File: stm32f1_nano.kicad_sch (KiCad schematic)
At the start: 48 parts, among them J1 Analog, J2 Digital, J3 TYPE-C-31-M-12, J4 Conn_ST_STDC14, Q1 AO3401A, Q3 AO3401A, U1 STM32F103C8T6, U2 W25Q32JVSS, U3 AMS1117-3.3, U5 AMS1117-5.0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

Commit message: First draft almost done
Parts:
- added J5: DEBUG, Connector_PinHeader_2.54mm:PinHeader_1x04_P2.54mm_Vertical, symbol Connector_Generic:Conn_01x04
- C15, C16, D7, J4, Q3, R11, U5: now not fitted
- J1, J2: now left out of the parts list
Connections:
- net GND: now also J5.1 (Pin_1)
- net SWCLK: now also J5.3 (Pin_3)
- net SWDIO: now also J5.4 (Pin_4)
- net SWO: now also J5.2 (Pin_2)
- net ~{RESET}: no longer J2.13 (Pin_13)
- no-connect marks 6 -> 7
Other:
- moved on the sheet: JP1

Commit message: New PS
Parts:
- removed JP1: Disc. VBUS, Jumper:SolderJumper-2_P1.3mm_Bridged_RoundedPad1.0x1.5mm, symbol Jumper:SolderJumper_2_Bridged
- added C17, C18: 1u 25V, Capacitor_SMD:C_0402_1005Metric, symbol Device:C_Small
- added D8: LED red (PWR), LED_SMD:LED_0603_1608Metric, symbol Device:LED_Small
- added D9: 1N5819WS, Diode_SMD:D_SOD-323, symbol Device:D_Schottky_Small
- added R12: 1k5, Resistor_SMD:R_0402_1005Metric, symbol Device:R_Small
- added U4: XC6206P332MR, Package_TO_SOT_SMD:SOT-23-3, symbol Regulator_Linear:XC6206PxxxMR
- C13, C14, D5, D6, Q1, R10, R9, U3: now not fitted; now left out of the parts list
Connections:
- net VBUS is gone; now on net +5V: Q1.3 (D)
- net +3.3V: now also C18.1, D8.2 (A), U4.2 (VO)
- net +5V: now also C17.1, D9.1 (K), U4.3 (VI)
- net GND: now also C17.2, C18.2, R12.2, U4.1 (GND)
- net VBUS0: now reaches J3.A4 (VBUS), J3.A9 (VBUS), J3.B4 (VBUS), J3.B9 (VBUS)
- net VBUS0: now also D9.2 (A)
- new net: D8.1 (K), R12.1
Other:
- note added: "3V3 Power Supply (Input: 15V)"
- note removed: "3V3 Power Supply"
- moved on the sheet: C15, C16, D7, JP2, Q3, R11, U5

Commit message: Reassigned Pins
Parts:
- removed C11: 20p 50V, Capacitor_SMD:C_0603_1608Metric, symbol Device:C_Small
- removed D7: 6V, Diode_SMD:D_MiniMELF, symbol Device:D_Zener_Small
- removed X1: NX3225GD-8MHZ-STD-CRA-3, Project_Library:NX3225GD8MHZSTDCRA3, symbol Project_Library:NX3225GD-8MHZ-STD-CRA-3
- added C19: 20p 50V, Capacitor_SMD:C_0402_1005Metric, symbol Device:C_Small
- added D10: SMF6.0CA, Diode_SMD:D_SOD-123F, symbol Device:D_Zener_Small
- added U6: SRV05-4, Package_TO_SOT_SMD:SOT-23-6, symbol Power_Protection:SRV05-4
- added Y1: X322516MLB4SI, Crystal:Crystal_SMD_3225-4Pin_3.2x2.5mm, symbol Device:Crystal_GND24_Small
- C10: footprint Capacitor_SMD:C_0603_1608Metric -> Capacitor_SMD:C_0402_1005Metric; JLCPCB Part # C1648 -> C1554; Manufacturer Samsung Electro-Mechanics -> FH (Guangdong Fenghua Advanced Tech); Partnumber CL10C200JB8NNNC -> 0402CG200J500NT
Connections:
- net +5V: now also D10.1 (K)
- net GND: now also C19.1, Y1.2, Y1.4
- net HSE_IN: now also C19.2, Y1.1; no longer C10.2
- net HSE_OUT: now also C10.2, Y1.3
- net LED2_ORG: now also U1.3 (PC14); no longer U1.38 (PA15)
- net LED3_RED: now also U1.29 (PA8); no longer U1.21 (PB10)
- net LED4_BLU: now also U1.20 (PB2); no longer U1.22 (PB11)
- net PB4: now also J2.10 (Pin_10); no longer J2.9 (Pin_9)
- net PB5: now also J2.9 (Pin_9); no longer J2.8 (Pin_8)
- net PB6: now also J2.8 (Pin_8); no longer J1.9 (Pin_9)
- net PB7: now also J2.7 (Pin_7); no longer J1.8 (Pin_8)
- net PB8: now also J2.6 (Pin_6); no longer J2.5 (Pin_5)
- net PB9: now also J2.5 (Pin_5); no longer J2.4 (Pin_4)
- net PC13: now also J2.4 (Pin_4); no longer J2.7 (Pin_7)
- net at Q3.1 (G), R11.1: now also D10.2 (A)
- removed net PA8: J2.10 (Pin_10), U1.29 (PA8)
- net PB2 renamed PA15
- net PA15: now also U1.38 (PA15); no longer U1.20 (PB2)
- removed net PC14: J2.6 (Pin_6), U1.3 (PC14)
- new net PB10: J1.9 (Pin_9), U1.21 (PB10)
- new net PB11: J1.8 (Pin_8), U1.22 (PB11)

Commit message: Almost done
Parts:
- removed D10: SMF6.0CA, Diode_SMD:D_SOD-123F, symbol Device:D_Zener_Small
- removed JP2: Disc. 12V PS, Jumper:SolderJumper-2_P1.3mm_Bridged_RoundedPad1.0x1.5mm, symbol Jumper:SolderJumper_2_Bridged
- removed Q3: AO3401A, Package_TO_SOT_SMD:SOT-23, symbol Transistor_FET:AO3401A
- removed R11: 100k, Resistor_SMD:R_0402_1005Metric, symbol Device:R_Small
- removed U6: SRV05-4, Package_TO_SOT_SMD:SOT-23-6, symbol Power_Protection:SRV05-4
- C12: now not fitted; now left out of the parts list
- C15, C16: now fitted
- U2: value W25Q32JVSS -> W25Q128JVSIQ; now not fitted
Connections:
- net +5V: now also C16.1, U5.2 (VO); no longer Q1.3 (D)
- net VBUS0 renamed VBUS
- net VBUS: now also Q1.3 (D)

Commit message: First Version released to production
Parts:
- removed R12: 1k5, Resistor_SMD:R_0402_1005Metric, symbol Device:R_Small
- added R11: 75, Resistor_SMD:R_0402_1005Metric, symbol Device:R_Small
- R1, R2, R3: value 1k5 -> 300; JLCPCB Part # C25867 -> C25102; Manufacturer_Part_Number 0402WGF1501TCE -> 0402WGF3000TCE; Partnumber 0402WGF1501TCE -> 0402WGF3000TCE
- R4: value 1k5 -> 75; JLCPCB Part # C25867 -> C25133; Manufacturer_Part_Number 0402WGF1501TCE -> 0402WGF750JTCE; Partnumber 0402WGF1501TCE -> 0402WGF750JTCE
- R9: value 1k5 -> 300; JLCPCB Part # C25867 -> C25102; Manufacturer_Part_Number 0402WGF1501TCE -> 0402WGF3000TCE; Partnumber 0402WGF1501TCE -> 0402WGF3000TCE; now fitted; now in the parts list
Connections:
- net +3.3V: now also R11.2; no longer R1.2
- net GND: now also R1.1, R9.1; no longer R9.2
- net PWR_LED_K: now also R9.2; no longer R9.1
- net at D1.2 (A): now also R11.1; no longer R1.1
- net at D8.1 (K): now also R1.2

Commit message: doc
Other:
- company: (none) -> easy-smart solution GmbH
- title: (none) -> STM32F1 Nano
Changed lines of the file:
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@@
   (paper "A4")
   (title_block
-    (date "sam. 04 avril 2015")
+    (title "STM32F1 Nano")
+    (date "2023-08-23")
+    (company "easy-smart solution GmbH")
   )
   (junction (at 130.175 41.275) (diameter 0) (color 0 0 0 0)

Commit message: #2 green and red LED are too bright
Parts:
- R1, R2, R3: value 300 -> 330; JLCPCB Part # C25102 -> C25104; Manufacturer_Name UNI-ROYAL(Uniroyal Elec) -> (none); Manufacturer_Part_Number 0402WGF3000TCE -> (none); Partnumber 0402WGF3000TCE -> 0402WGF3300TCE
- R11: value 75 -> 200; JLCPCB Part # C25133 -> C25087; Manufacturer_Name UNI-ROYAL(Uniroyal Elec) -> (none); Manufacturer_Part_Number 0402WGF750JTCE -> (none); Partnumber 0402WGF750JTCE -> 0402WGF2000TCE
- R4: value 75 -> 150; JLCPCB Part # C25133 -> C25082; Manufacturer_Name UNI-ROYAL(Uniroyal Elec) -> (none); Manufacturer_Part_Number 0402WGF750JTCE -> (none); Partnumber 0402WGF750JTCE -> 0402WGF1500TCE
- R9: value 300 -> 330; JLCPCB Part # C25102 -> C25104; Manufacturer_Name UNI-ROYAL(Uniroyal Elec) -> (none); Manufacturer_Part_Number 0402WGF3000TCE -> (none); Partnumber 0402WGF3000TCE -> 0402WGF3300TCE; now not fitted; now left out of the parts list
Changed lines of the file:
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@@
       (effects (font (size 1 1)))
     )
-    (property "Value" "300" (at 84.455 153.035 90)
+    (property "Value" "330" (at 84.455 153.035 90)
       (effects (font (size 1 1)))
     )
@@
       (effects (font (size 1.27 1.27)) hide)
     )
-    (property "Description" "62.5mW Thick Film Resistors ±100ppm/℃ ±1% 300Ω 0402  Chip Resistor - Surface Mount ROHS" (at 82.55 153.035 0)
-      (effects (font (size 1.27 1.27)) hide)
-    )
-    (property "JLCPCB Part #" "C25102" (at 82.55 153.035 0)
+    (property "Description" "62.5mW Thick Film Resistors ±100ppm/℃ ±1% 330Ω 0402  Chip Resistor - Surface Mount ROHS" (at 82.55 153.035 0)
+      (effects (font (size 1.27 1.27)) hide)
+    )
+    (property "JLCPCB Part #" "C25104" (at 82.55 153.035 0)
       (effects (font (size 1.27 1.27)) hide)
     )
@@
       (effects (font (size 1.27 1.27)) hide)
     )
-    (property "Manufacturer_Part_Number" "0402WGF3000TCE" (at 82.55 153.035 0)
-      (effects (font (size 1.27 1.27)) hide)
-    )
-    (property "Partnumber" "0402WGF3000TCE" (at 82.55 153.035 0)
-      (effects (font (size 1.27 1.27)) hide)
-    )
-    (property "Manufacturer_Name" "UNI-ROYAL(Uniroyal Elec)" (at 82.55 153.035 0)
+    (property "Partnumber" "0402WGF3300TCE" (at 82.55 153.035 0)
       (effects (font (size 1.27 1.27)) hide)
     )
@@
       (effects (font (size 1 1)))
     )
-    (property "Value" "75" (at 263.525 34.29 90)
+    (property "Value" "150" (at 263.525 34.29 90)
       (effects (font (size 1 1)))
     )
@@
       (effects (font (size 1.27 1.27)) hide)
     )
-    (property "Description" "62.5mW Thick Film Resistors ±100ppm/℃ ±1% 75Ω 0402  Chip Resistor - Surface Mount ROHS" (at 261.62 34.29 0)
-      (effects (font (size 1.27 1.27)) hide)
-    )
-    (property "JLCPCB Part #" "C25133" (at 261.62 34.29 0)
+    (property "Description" "62.5mW Thick Film Resistors ±100ppm/℃ ±1% 150Ω 0402  Chip Resistor - Surface Mount ROHS" (at 261.62 34.29 0)
+      (effects (font (size 1.27 1.27)) hide)
+    )
+    (property "JLCPCB Part #" "C25082" (at 261.62 34.29 0)
       (effects (font (size 1.27 1.27)) hide)
     )
@@
       (effects (font (size 1.27 1.27)) hide)
     )
-    (property "Manufacturer_Part_Number" "0402WGF750JTCE" (at 261.62 34.29 0)
-      (effects (font (size 1.27 1.27)) hide)
-    )
-    (property "Partnumber" "0402WGF750JTCE" (at 261.62 34.29 0)
-      (effects (font (size 1.27 1.27)) hide)
-    )
-    (property "Manufacturer_Name" "UNI-ROYAL(Uniroyal Elec)" (at 261.62 34.29 0)
+    (property "Partnumber" "0402WGF1500TCE" (at 261.62 34.29 0)
       (effects (font (size 1.27 1.27)) hide)
     )
@@
       (effects (font (size 1 1)))
     )
-    (property "Value" "300" (at 247.65 34.29 90)
+    (property "Value" "330" (at 247.65 34.29 90)
       (effects (font (size 1 1)))
     )
@@
       (effects (font (size 1.27 1.27)) hide)
     )
-    (property "Description" "62.5mW Thick Film Resistors ±100ppm/℃ ±1% 300Ω 0402  Chip Resistor - Surface Mount ROHS" (at 245.745 34.29 0)
-      (effects (font (size 1.27 1.27)) hide)
-    )
-    (property "JLCPCB Part #" "C25102" (at 245.745 34.29 0)
+    (property "Description" "62.5mW Thick Film Resistors ±100ppm/℃ ±1% 330Ω 0402  Chip Resistor - Surface Mount ROHS" (at 245.745 34.29 0)
+      (effects (font (size 1.27 1.27)) hide)
+    )
+    (property "JLCPCB Part #" "C25104" (at 245.745 34.29 0)
       (effects (font (size 1.27 1.27)) hide)
     )
@@
       (effects (font (size 1.27 1.27)) hide)
     )
-    (property "Manufacturer_Part_Number" "0402WGF3000TCE" (at 245.745 34.29 0)
-      (effects (font (size 1.27 1.27)) hide)
-    )
-    (property "Partnumber" "0402WGF3000TCE" (at 245.745 34.29 0)
-      (effects (font (size 1.27 1.27)) hide)
-    )
-    (property "Manufacturer_Name" "UNI-ROYAL(Uniroyal Elec)" (at 245.745 34.29 0)
+    (property "Partnumber" "0402WGF3300TCE" (at 245.745 34.29 0)
       (effects (font (size 1.27 1.27)) hide)
     )
@@
       (effects (font (size 1 1)))
     )
-    (property "Value" "300" (at 255.27 34.29 90)
+    (property "Value" "330" (at 255.27 34.29 90)
       (effects (font (size 1 1)))
     )
@@
       (effects (font (size 1.27 1.27)) hide)
     )
-    (property "Description" "62.5mW Thick Film Resistors ±100ppm/℃ ±1% 300Ω 0402  Chip Resistor - Surface Mount ROHS" (at 253.365 34.29 0)
-      (effects (font (size 1.27 1.27)) hide)
-    )
-    (property "JLCPCB Part #" "C25102" (at 253.365 34.29 0)
+    (property "Description" "62.5mW Thick Film Resistors ±100ppm/℃ ±1% 330Ω 0402  Chip Resistor - Surface Mount ROHS" (at 253.365 34.29 0)
+      (effects (font (size 1.27 1.27)) hide)
+    )
+    (property "JLCPCB Part #" "C25104" (at 253.365 34.29 0)
       (effects (font (size 1.27 1.27)) hide)
     )
@@
       (effects (font (size 1.27 1.27)) hide)
     )
-    (property "Manufacturer_Part_Number" "0402WGF3000TCE" (at 253.365 34.29 0)
-      (effects (font (size 1.27 1.27)) hide)
-    )
-    (property "Partnumber" "0402WGF3000TCE" (at 253.365 34.29 0)
-      (effects (font (size 1.27 1.27)) hide)
-    )
-    (property "Manufacturer_Name" "UNI-ROYAL(Uniroyal Elec)" (at 253.365 34.29 0)
+    (property "Partnumber" "0402WGF3300TCE" (at 253.365 34.29 0)
       (effects (font (size 1.27 1.27)) hide)
     )
@@
       (effects (font (size 1 1)))
     )
-    (property "Value" "75" (at 240.03 34.29 90)
+    (property "Value" "200" (at 240.03 34.29 90)
       (effects (font (size 1 1)))
     )
@@
       (effects (font (size 1.27 1.27)) hide)
     )
-    (property "Description" "62.5mW Thick Film Resistors ±100ppm/℃ ±1% 75Ω 0402  Chip Resistor - Surface Mount ROHS" (at 238.125 34.29 0)
-      (effects (font (size 1.27 1.27)) hide)
-    )
-    (property "JLCPCB Part #" "C25133" (at 238.125 34.29 0)
+    (property "Description" "62.5mW Thick Film Resistors ±100ppm/℃ ±1% 200Ω 0402  Chip Resistor - Surface Mount ROHS" (at 238.125 34.29 0)
+      (effects (font (size 1.27 1.27)) hide)
+    )
+    (property "JLCPCB Part #" "C25087" (at 238.125 34.29 0)
       (effects (font (size 1.27 1.27)) hide)
     )
@@
       (effects (font (size 1.27 1.27)) hide)
     )
-    (property "Manufacturer_Part_Number" "0402WGF750JTCE" (at 238.125 34.29 0)
-      (effects (font (size 1.27 1.27)) hide)
-    )
-    (property "Partnumber" "0402WGF750JTCE" (at 238.125 34.29 0)
-      (effects (font (size 1.27 1.27)) hide)
-    )
-    (property "Manufacturer_Name" "UNI-ROYAL(Uniroyal Elec)" (at 238.125 34.29 0)
+    (property "Partnumber" "0402WGF2000TCE" (at 238.125 34.29 0)
       (effects (font (size 1.27 1.27)) hide)
     )
@@
   )
   (symbol (lib_id "Device:R_Small") (at 81.915 113.665 180) (unit 1)
-    (in_bom yes) (on_board yes) (dnp no)
+    (in_bom no) (on_board no) (dnp yes)
     (property "Reference" "R9" (at 80.01 113.665 90)
       (effects (font (size 1 1)))
     )
-    (property "Value" "300" (at 83.82 113.665 90)
+    (property "Value" "330" (at 83.82 113.665 90)
       (effects (font (size 1 1)))
     )
@@
       (effects (font (size 1.27 1.27)) hide)
     )
-    (property "Description" "62.5mW Thick Film Resistors ±100ppm/℃ ±1% 300Ω 0402  Chip Resistor - Surface Mount ROHS" (at 81.915 113.665 0)
-      (effects (font (size 1.27 1.27)) hide)
-    )
-    (property "JLCPCB Part #" "C25102" (at 81.915 113.665 0)
+    (property "Description" "62.5mW Thick Film Resistors ±100ppm/℃ ±1% 330Ω 0402  Chip Resistor - Surface Mount ROHS" (at 81.915 113.665 0)
+      (effects (font (size 1.27 1.27)) hide)
+    )
+    (property "JLCPCB Part #" "C25104" (at 81.915 113.665 0)
       (effects (font (size 1.27 1.27)) hide)
     )
@@
       (effects (font (size 1.27 1.27)) hide)
     )
-    (property "Manufacturer_Part_Number" "0402WGF3000TCE" (at 81.915 113.665 0)
-      (effects (font (size 1.27 1.27)) hide)
-    )
-    (property "Partnumber" "0402WGF3000TCE" (at 81.915 113.665 0)
-      (effects (font (size 1.27 1.27)) hide)
-    )
-    (property "Manufacturer_Name" "UNI-ROYAL(Uniroyal Elec)" (at 81.915 113.665 0)
-      (effects (font (size 1.27 1.27)) hide)
-    )
+    (property "Partnumber" "0402WGF3300TCE" (at 81.915 113.665 0)
+      (effects (font (size 1.27 1.27)) hide)
+    )

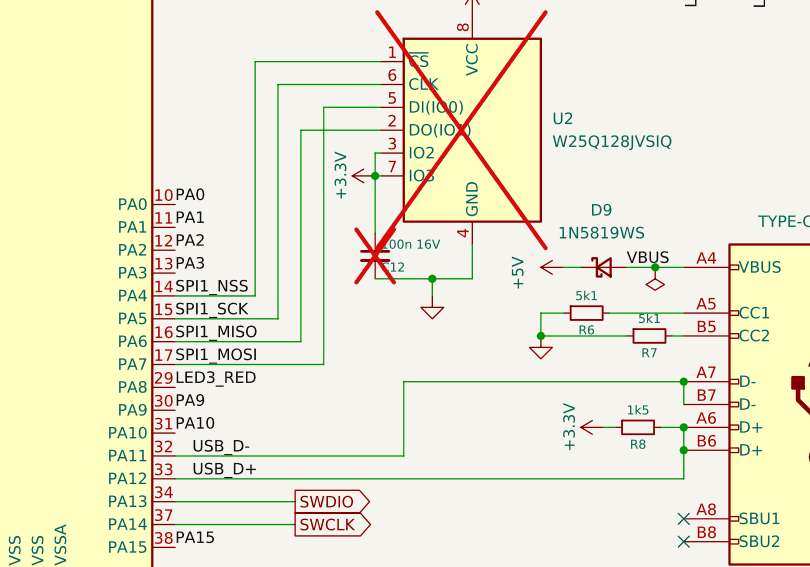
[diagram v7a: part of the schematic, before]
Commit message: #3 Make C12 bigger or move to Front
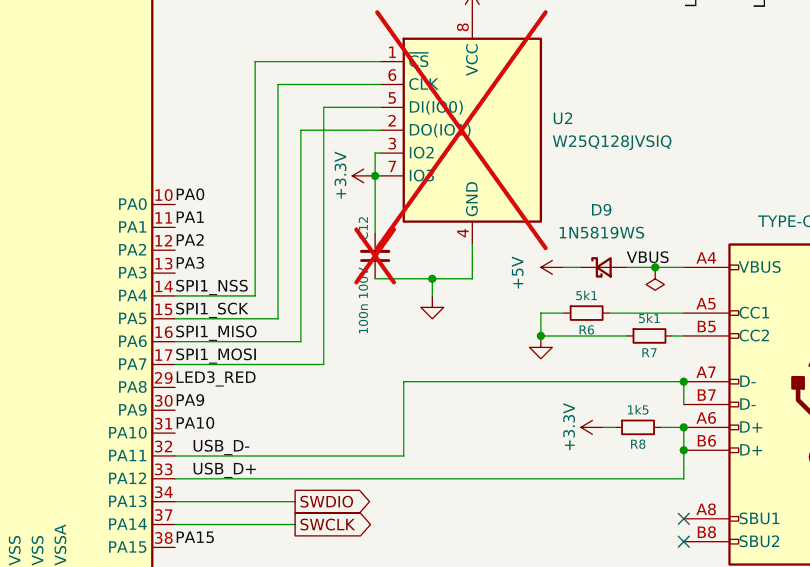
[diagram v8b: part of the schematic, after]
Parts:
- C12: value 100n 16V -> 100n 100V; footprint Capacitor_SMD:C_0402_1005Metric -> Capacitor_SMD:C_0805_2012Metric; JLCPCB Part # C1525 -> C28233; Manufacturer_Name (none) -> Samsung Electro-Mechanics; Manufacturer_Part_Number (none) -> CL21B104KCFNNNE; Partnumber CL05B104KO5NNNC -> CL21B104KCFNNNE
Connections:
- net +3.3V: now also C12.2; no longer C12.1
- net GND: now also C12.1; no longer C12.2
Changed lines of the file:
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@@
+    )
+  )
+  (symbol (lib_id "Device:C_Small") (at 201.93 80.01 180) (unit 1)
+    (in_bom no) (on_board no) (dnp yes)
+    (property "Reference" "C12" (at 200.66 75.565 90)
+      (effects (font (size 1 1)) (justify left))
+    )
+    (property "Value" "100n 100V" (at 200.66 81.28 90)
+      (effects (font (size 1 1)) (justify left))
+    )
+    (property "Footprint" "Capacitor_SMD:C_0805_2012Metric" (at 201.93 80.01 0)
+      (effects (font (size 1.27 1.27)) hide)
+    )
+    (property "Datasheet" "~" (at 201.93 80.01 0)
+      (effects (font (size 1.27 1.27)) hide)
+    )
+    (property "Manufacturer_Part_Number" "CL21B104KCFNNNE" (at 201.93 80.01 0)
+      (effects (font (size 1.27 1.27)) hide)
+    )
+    (property "Description" "100V 100nF X7R ±10% 0805  Multilayer Ceramic Capacitors MLCC - SMD/SMT ROHS" (at 201.93 80.01 0)
+      (effects (font (size 1.27 1.27)) hide)
+    )
+    (property "JLCPCB Part #" "C28233" (at 201.93 80.01 0)
+      (effects (font (size 1.27 1.27)) hide)
+    )
+    (property "Manufacturer" "Samsung Electro-Mechanics" (at 201.93 80.01 0)
+      (effects (font (size 1.27 1.27)) hide)
+    )
+    (property "Partnumber" "CL21B104KCFNNNE" (at 201.93 80.01 0)
+      (effects (font (size 1.27 1.27)) hide)
+    )
+    (property "Manufacturer_Name" "Samsung Electro-Mechanics" (at 201.93 80.01 0)
+      (effects (font (size 1.27 1.27)) hide)
+    )
+    (property "isBasicPart" "YES" (at 201.93 80.01 0)
+      (effects (font (size 1.27 1.27)) hide)
+    )
+    (pin "1")
+    (pin "2")
+    (instances
+      (project "stm32f1_nano"
+        (path "/0d35483a-0b12-46cc-b9f2-896fd6831779"
+          (reference "C12") (unit 1)
+        )
+      )
+      (project "stm32f407vg"
+        (path "/2d452db2-a0cd-4a57-9497-df1dd0591a30"
+          (reference "C125") (unit 1)
+        )
+        (path "/2d452db2-a0cd-4a57-9497-df1dd0591a30/cb9cd892-4fab-4f54-9695-d8ba54556bb0"
+          (reference "C245") (unit 1)
+        )
+        (path "/2d452db2-a0cd-4a57-9497-df1dd0591a30/480569e0-5dbc-4314-a9d6-1dbd834f5833"
+          (reference "C501") (unit 1)
+        )
+      )
+      (project "basicparts"
+        (path "/43a31acf-2604-4bbd-9556-e633c3dff6c4"
+          (reference "C103") (unit 1)
+        )
+      )
     )
   )
@@
   )
   (symbol (lib_id "Memory_Flash:W25Q32JVSS") (at 212.725 66.04 0) (unit 1)
-    (in_bom no) (on_board yes) (dnp yes) (fields_autoplaced)
+    (in_bom no) (on_board no) (dnp yes) (fields_autoplaced)
     (property "Reference" "U2" (at 221.615 64.77 0)
       (effects (font (size 1.27 1.27)) (justify left))
@@
     )
   )
-  (symbol (lib_id "Device:C_Small") (at 201.93 80.01 0) (unit 1)
-    (in_bom no) (on_board yes) (dnp yes)
-    (property "Reference" "C12" (at 202.565 81.28 0)
-      (effects (font (size 1 1)) (justify left))
-    )
-    (property "Value" "100n 16V" (at 202.565 78.74 0)
-      (effects (font (size 1 1)) (justify left))
-    )
-    (property "Footprint" "Capacitor_SMD:C_0402_1005Metric" (at 201.93 80.01 0)
-      (effects (font (size 1.27 1.27)) hide)
-    )
-    (property "Datasheet" "~" (at 201.93 80.01 0)
-      (effects (font (size 1.27 1.27)) hide)
-    )
-    (property "Description" "16V 100nF X7R ±10% 0402  Multilayer Ceramic Capacitors MLCC - SMD/SMT ROHS" (at 201.93 80.01 0)
-      (effects (font (size 1.27 1.27)) hide)
-    )
-    (property "JLCPCB Part #" "C1525" (at 201.93 80.01 0)
-      (effects (font (size 1.27 1.27)) hide)
-    )
-    (property "Manufacturer" "Samsung Electro-Mechanics" (at 201.93 80.01 0)
-      (effects (font (size 1.27 1.27)) hide)
-    )
-    (property "Partnumber" "CL05B104KO5NNNC" (at 201.93 80.01 0)
-      (effects (font (size 1.27 1.27)) hide)
-    )
-    (property "isBasicPart" "YES" (at 201.93 80.01 0)
-      (effects (font (size 1.27 1.27)) hide)
-    )
-    (pin "1")
-    (pin "2")
-    (instances
-      (project "stm32f1_nano"
-        (path "/0d35483a-0b12-46cc-b9f2-896fd6831779"
-          (reference "C12") (unit 1)
-        )
-      )
-      (project "stm32f407vg"
-        (path "/2d452db2-a0cd-4a57-9497-df1dd0591a30"
-          (reference "C129") (unit 1)
-        )
-        (path "/2d452db2-a0cd-4a57-9497-df1dd0591a30/cb9cd892-4fab-4f54-9695-d8ba54556bb0"
-          (reference "C249") (unit 1)
-        )
-        (path "/2d452db2-a0cd-4a57-9497-df1dd0591a30/480569e0-5dbc-4314-a9d6-1dbd834f5833"
-          (reference "C503") (unit 1)
-        )
-      )
-      (project "basicparts"
-        (path "/43a31acf-2604-4bbd-9556-e633c3dff6c4"
-          (reference "C105") (unit 1)
-        )
-      )
-    )
-  )
   (symbol (lib_id "Device:C_Small") (at 68.58 113.665 0) (unit 1)
     (in_bom no) (on_board no) (dnp yes) (fields_autoplaced)
@@
   )
   (symbol (lib_id "Regulator_Linear:AMS1117-3.3") (at 52.07 173.99 0) (unit 1)
-    (in_bom yes) (on_board yes) (dnp yes) (fields_autoplaced)
+    (in_bom yes) (on_board no) (dnp yes) (fields_autoplaced)
     (property "Reference" "U5" (at 52.07 167.005 0)
       (effects (font (size 1.27 1.27)))
